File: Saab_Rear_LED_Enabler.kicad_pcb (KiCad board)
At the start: 2 copper layers, 100 x 50 mm, 1 part

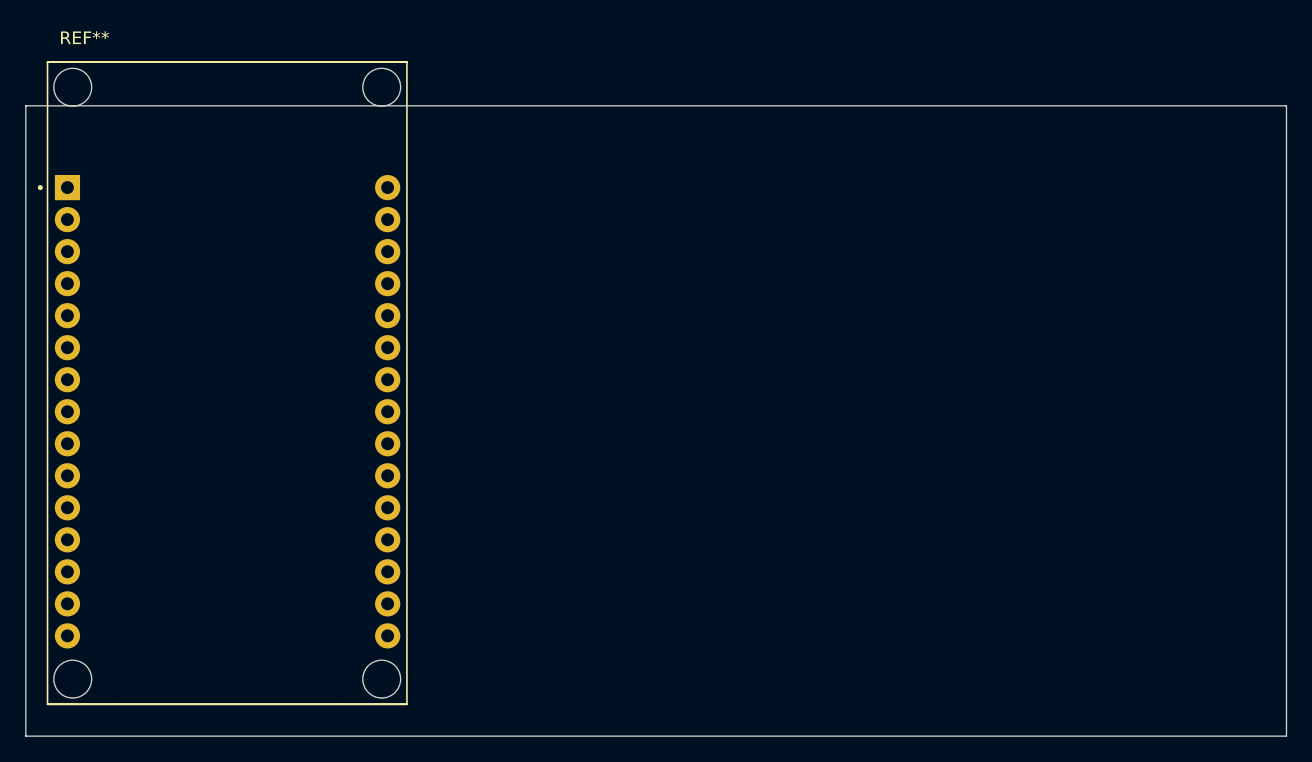
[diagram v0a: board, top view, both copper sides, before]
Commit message: LED Enabler updated to v0.80, see Changelog for details
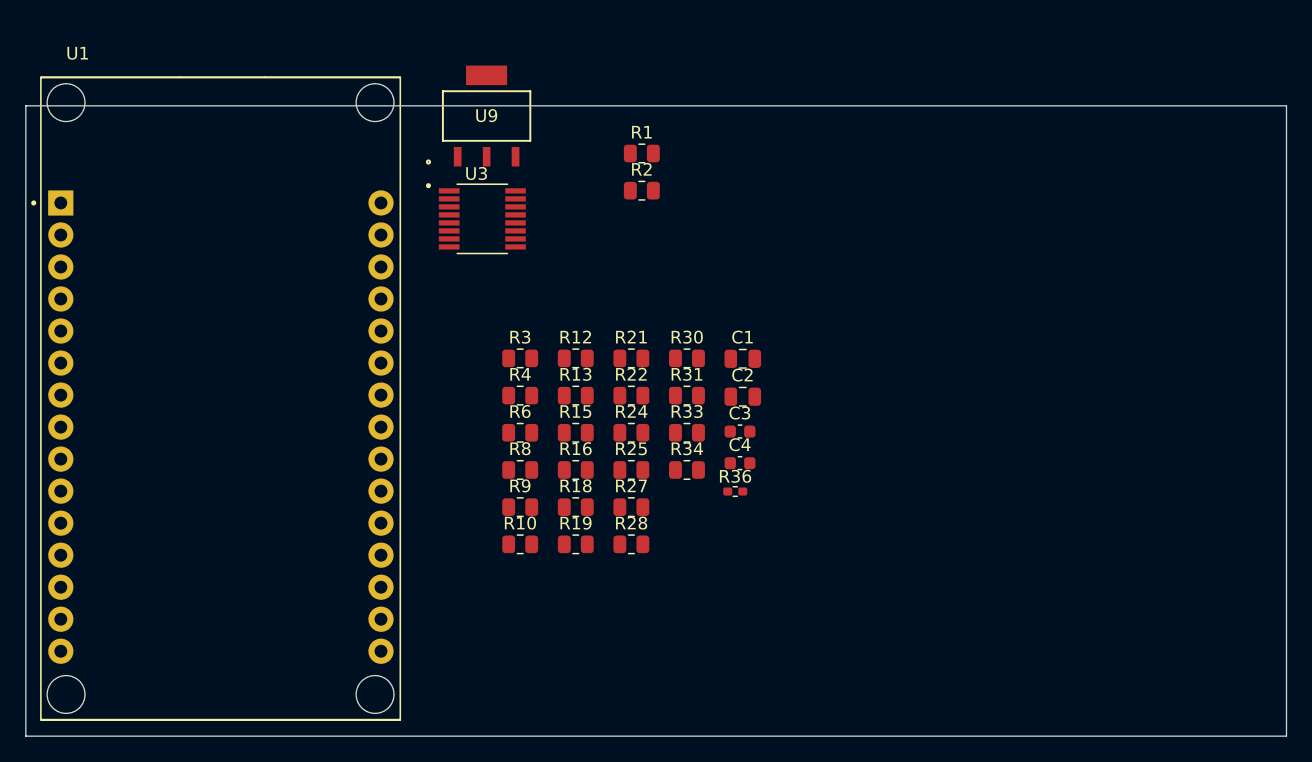
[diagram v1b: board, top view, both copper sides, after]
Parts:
- removed REF**: ESP32_DEVKIT_V1_30PIN, czabel_personal:ESP32_DEVKIT_V1_30PIN
- added C1: 10u, Capacitor_SMD:C_0805_2012Metric, F.Cu at (146.9, 100.1)
- added C2: 10u, Capacitor_SMD:C_0805_2012Metric, F.Cu at (146.9, 103.1)
- added C3: 0.1u, Capacitor_SMD:C_0603_1608Metric, F.Cu at (146.7, 105.8)
- added C4: 0.1u, Capacitor_SMD:C_0603_1608Metric, F.Cu at (146.7, 108.3)
- added R1: 2.4k, Resistor_SMD:R_0805_2012Metric, F.Cu at (138.9, 83.8)
- added R10: 150, Resistor_SMD:R_0805_2012Metric, F.Cu at (129.2, 114.8)
- added R12: 1.5k, Resistor_SMD:R_0805_2012Metric, F.Cu at (133.6, 100.0)
- added R13: 150, Resistor_SMD:R_0805_2012Metric, F.Cu at (133.6, 103.0)
- added R15: 1.5k, Resistor_SMD:R_0805_2012Metric, F.Cu at (133.6, 105.9)
- added R16: 150, Resistor_SMD:R_0805_2012Metric, F.Cu at (133.6, 108.9)
- added R18: 1.5k, Resistor_SMD:R_0805_2012Metric, F.Cu at (133.6, 111.8)
- added R19: 150, Resistor_SMD:R_0805_2012Metric, F.Cu at (133.6, 114.8)
- added R2: 2.4k, Resistor_SMD:R_0805_2012Metric, F.Cu at (138.9, 86.7)
- added R21: 1.5k, Resistor_SMD:R_0805_2012Metric, F.Cu at (138.0, 100.0)
- added R22: 150, Resistor_SMD:R_0805_2012Metric, F.Cu at (138.0, 103.0)
- added R24: 150, Resistor_SMD:R_0805_2012Metric, F.Cu at (138.0, 105.9)
- added R25: 1.5k, Resistor_SMD:R_0805_2012Metric, F.Cu at (138.0, 108.9)
- added R27: 150, Resistor_SMD:R_0805_2012Metric, F.Cu at (138.0, 111.8)
- added R28: 1.5k, Resistor_SMD:R_0805_2012Metric, F.Cu at (138.0, 114.8)
- added R3: 1.5k, Resistor_SMD:R_0805_2012Metric, F.Cu at (129.2, 100.0)
- added R30: 150, Resistor_SMD:R_0805_2012Metric, F.Cu at (142.4, 100.0)
- added R31: 1.5k, Resistor_SMD:R_0805_2012Metric, F.Cu at (142.4, 103.0)
- added R33: 150, Resistor_SMD:R_0805_2012Metric, F.Cu at (142.4, 105.9)
- added R34: 1.5k, Resistor_SMD:R_0805_2012Metric, F.Cu at (142.4, 108.9)
- added R36: 2k, Resistor_SMD:R_0402_1005Metric_Pad0.72x0.64mm_HandSolder, F.Cu at (146.3, 110.6)
- added R4: 150, Resistor_SMD:R_0805_2012Metric, F.Cu at (129.2, 103.0)
- added R6: 1.5k, Resistor_SMD:R_0805_2012Metric, F.Cu at (129.2, 105.9)
- added R8: 150, Resistor_SMD:R_0805_2012Metric, F.Cu at (129.2, 108.9)
- added R9: 1.5k, Resistor_SMD:R_0805_2012Metric, F.Cu at (129.2, 111.8)
- added U1: ESP32-DEVKIT-V1, czabel_personal:ESP32_DEVKIT_V1_30PIN, F.Cu at (105.5, 103.2)
- added U3: MAX11611EEET, czabel_personal:SOP63P602X175-16N, F.Cu at (126.2, 89.0)
- added U9: NCP1117ST50T3G, czabel_personal:SOT223-3_ONS, F.Cu at (126.5, 80.8)
